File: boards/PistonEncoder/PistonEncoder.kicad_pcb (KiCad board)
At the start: 2 copper layers, 150 x 100 mm, 32 parts, among them J1 ISP, J2 Ext, J3 PWR, J4 LED1, J5 LED2, J6 Pistons1, J7 Pistons2, J8 BoardCon, Q1 BC547, U1 ATmega48-20P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

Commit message: Added bypass caps to power supplies, use cheaper MAX232 IC.
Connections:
- U2 pad 10: /LED_PWR -> unconnected-(U2-COM-Pad10)
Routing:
- net /LED_PWR: track 202.2 -> 195.2 mm
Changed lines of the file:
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@@
 	(net 75 "unconnected-(U5-O6-Pad9)")
 	(net 76 "Net-(Q1-B)")
+	(net 77 "unconnected-(U2-COM-Pad10)")
 	(footprint "Connector_IDC:IDC-Header_2x05_P2.54mm_Vertical"
 		(layer "F.Cu")
@@
 			(layers "*.Cu" "*.Mask")
 			(remove_unused_layers no)
-			(net 22 "/LED_PWR")
+			(net 77 "unconnected-(U2-COM-Pad10)")
 			(pinfunction "COM")
-			(pintype "passive")
+			(pintype "passive+no_connect")
 		)
 		(pad "11" thru_hole oval
@@
 		(tags "TO-92L Inline Wide transistor")
 		(property "Reference" "Q1"
-			(at 2.54 -3.56 270)
+			(at 2.54 -3.56 -90)
 			(layer "F.SilkS")
 			(effects
@@
 		)
 		(property "Value" "BC547"
-			(at 2.54 2.79 270)
+			(at 2.54 2.79 -90)
 			(layer "F.Fab")
 			(effects
@@
 		)
 		(fp_text user "${REFERENCE}"
-			(at 2.54 0 270)
+			(at 2.54 0 -90)
 			(layer "F.Fab")
 			(effects
@@
 	)
 	(segment
-		(start 112.776 59.896)
-		(end 121.158 68.278)
+		(start 115.062 99.187)
+		(end 119.507 99.187)
 		(width 0.6)
 		(layer "B.Cu")
@@
 	)
 	(segment
-		(start 134.62 58.42)
-		(end 133.096 56.896)
-		(width 0.6)
-		(layer "B.Cu")
-		(net 22)
-	)
-	(segment
-		(start 113.538 106.68)
-		(end 113.538 105.41)
+		(start 119.507 99.187)
+		(end 121.158 97.536)
 		(width 0.6)
 		(layer "B.Cu")
@@
 	)
 	(segment
-		(start 109.22 101.092)
-		(end 109.22 99.06)
+		(start 121.158 97.536)
+		(end 121.158 68.278)
 		(width 0.6)
 		(layer "B.Cu")
@@
 	)
 	(segment
-		(start 119.634 99.06)
-		(end 109.22 99.06)
+		(start 113.538 100.711)
+		(end 115.062 99.187)
 		(width 0.6)
 		(layer "B.Cu")
@@
 	)
 	(segment
-		(start 112.776 56.896)
-		(end 112.776 59.896)
+		(start 205.74 130.115919)
+		(end 200.338081 124.714)
 		(width 0.6)
 		(layer "B.Cu")
@@
 	(segment
 		(start 133.096 56.896)
-		(end 112.776 56.896)
+		(end 134.62 58.42)
 		(width 0.6)
 		(layer "B.Cu")
@@
 	)
 	(segment
-		(start 121.158 97.536)
-		(end 119.634 99.06)
+		(start 205.74 131.318)
+		(end 205.74 130.115919)
 		(width 0.6)
 		(layer "B.Cu")
@@
 	)
 	(segment
-		(start 121.158 68.278)
-		(end 121.158 97.536)
+		(start 112.776 59.896)
+		(end 112.776 56.896)
 		(width 0.6)
 		(layer "B.Cu")
@@
 	)
 	(segment
-		(start 205.74 130.115919)
-		(end 200.338081 124.714)
+		(start 121.158 68.278)
+		(end 112.776 59.896)
 		(width 0.6)
 		(layer "B.Cu")
@@
 	)
 	(segment
-		(start 205.74 131.318)
-		(end 205.74 130.115919)
+		(start 112.776 56.896)
+		(end 133.096 56.896)
 		(width 0.6)
 		(layer "B.Cu")
@@
 	)
 	(segment
-		(start 113.538 105.41)
-		(end 109.22 101.092)
+		(start 200.338081 124.714)
+		(end 113.538 124.714)
 		(width 0.6)
 		(layer "B.Cu")
@@
 	)
 	(segment
-		(start 200.338081 124.714)
-		(end 113.538 124.714)
+		(start 113.538 106.68)
+		(end 113.538 100.711)
 		(width 0.6)
 		(layer "B.Cu")

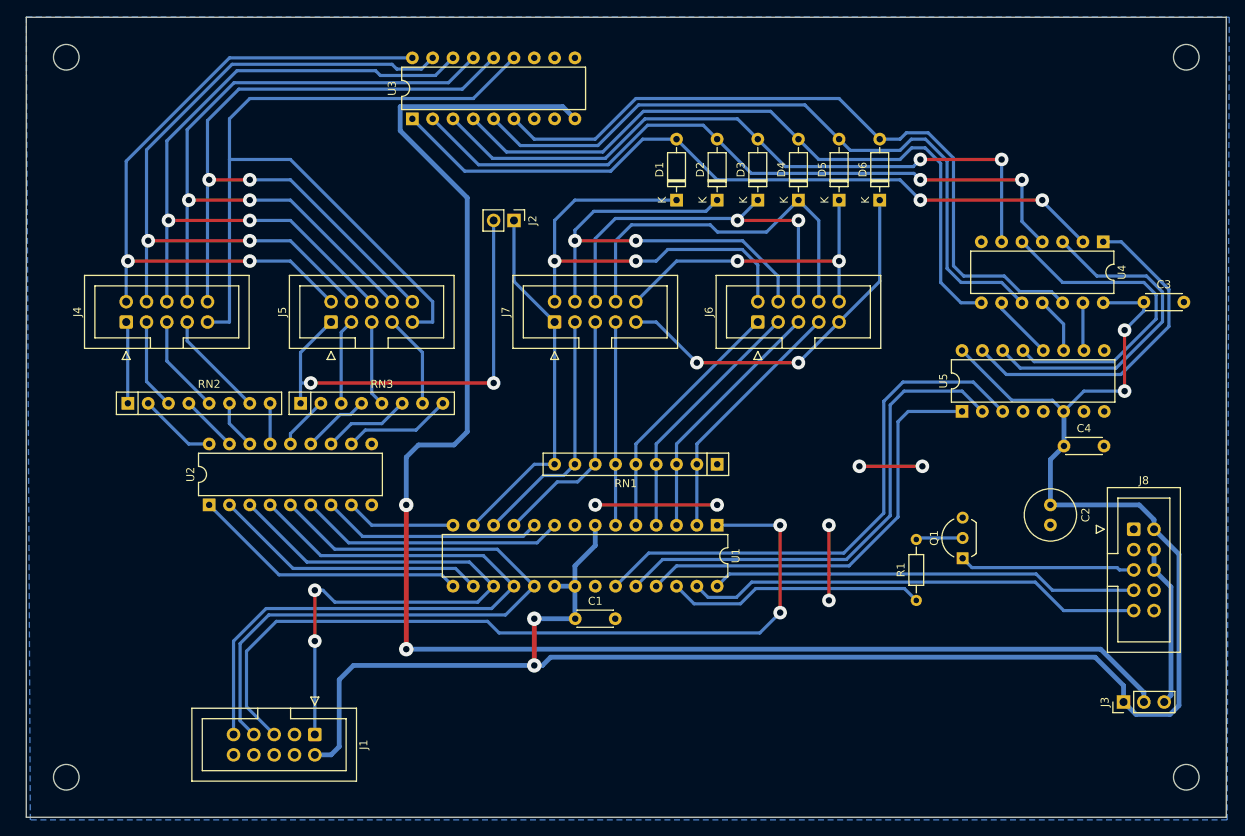
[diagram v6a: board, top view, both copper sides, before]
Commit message: Updated design rules to 0.32mm template and exported Gerber files
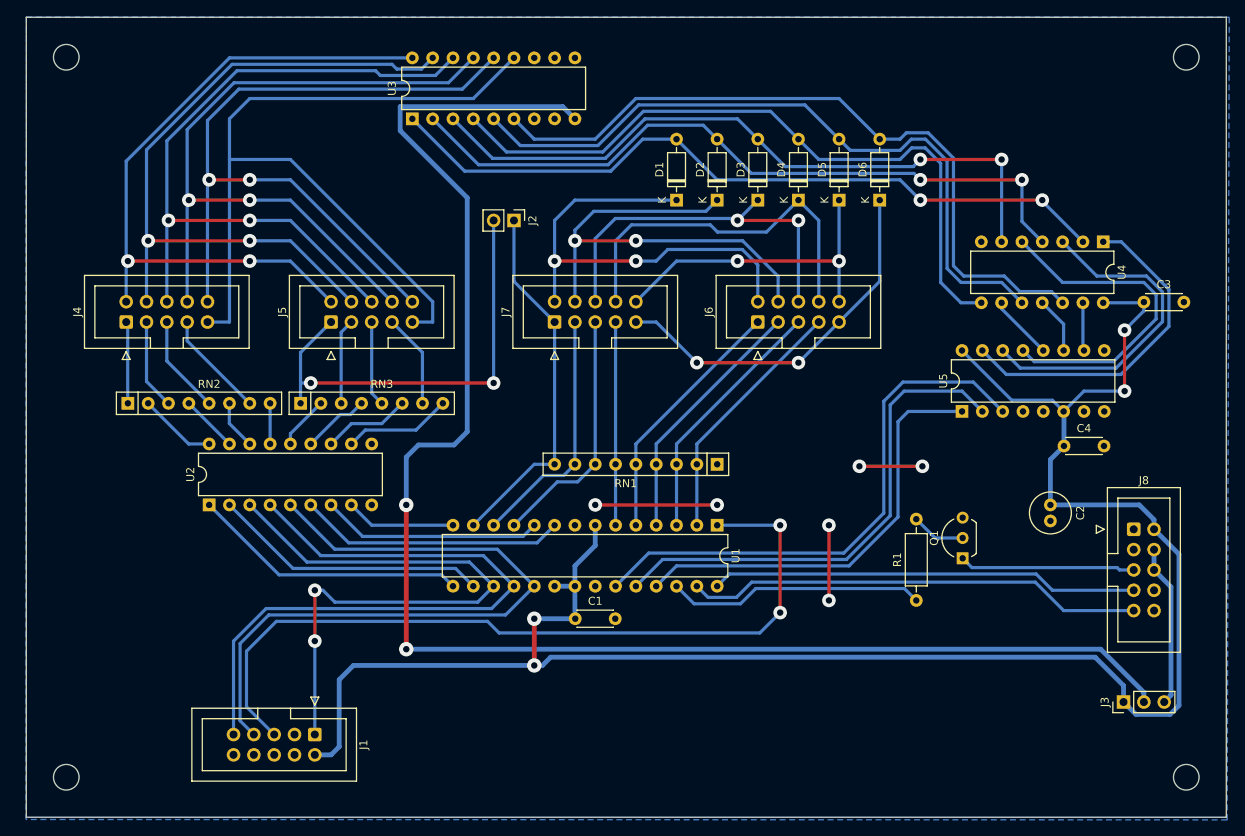
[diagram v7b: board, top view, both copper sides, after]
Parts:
- C2: footprint Capacitor_THT:C_Radial_D6.3mm_H7.0mm_P2.50mm -> Capacitor_THT:C_Radial_D5.0mm_H11.0mm_P2.00mm
- R1: footprint Resistor_THT:R_Axial_DIN0204_L3.6mm_D1.6mm_P7.62mm_Horizontal -> Resistor_THT:R_Axial_DIN0207_L6.3mm_D2.5mm_P10.16mm_Horizontal
- RN1: value R_Network08 -> 10k
- RN2, RN3: value R_Pack04_SIP_Split -> 330
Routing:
- net Net-(Q1-B): track 5.61 -> 6.77 mm
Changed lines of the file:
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@@
 		(pad_to_mask_clearance 0)
 		(allow_soldermask_bridges_in_footprints no)
-		(aux_axis_origin 66.04 45.72)
+		(aux_axis_origin 66.04 145.72)
 		(pcbplotparams
-			(layerselection 0x00010fc_ffffffff)
+			(layerselection 0x0001060_fffffffe)
 			(plot_on_all_layers_selection 0x0000000_00000000)
 			(disableapertmacros no)
@@
 			(viasonmask no)
 			(mode 1)
-			(useauxorigin no)
+			(useauxorigin yes)
 			(hpglpennumber 1)
 			(hpglpenspeed 20)
@@
 			(outputformat 1)
 			(mirror no)
-			(drillshape 1)
+			(drillshape 0)
 			(scaleselection 1)
-			(outputdirectory "")
+			(outputdirectory "gerber/")
 		)
 	)
@@
 			)
 		)
-		(property "Value" "R_Pack04_SIP_Split"
+		(property "Value" "330"
 			(at 10.16 2.4 0)
 			(layer "F.Fab")
@@
 		)
 	)
-	(footprint "Resistor_THT:R_Axial_DIN0204_L3.6mm_D1.6mm_P7.62mm_Horizontal"
+	(footprint "Resistor_THT:R_Axial_DIN0207_L6.3mm_D2.5mm_P10.16mm_Horizontal"
 		(layer "F.Cu")
 		(at 177.292 118.618 90)
-		(descr "Resistor, Axial_DIN0204 series, Axial, Horizontal, pin pitch=7.62mm, 0.167W, length*diameter=3.6*1.6mm^2, http://cdn-reichelt.de/documents/datenblatt/B400/1_4W%23YAG.pdf")
-		(tags "Resistor Axial_DIN0204 series Axial Horizontal pin pitch 7.62mm 0.167W length 3.6mm diameter 1.6mm")
+		(descr "Resistor, Axial_DIN0207 series, Axial, Horizontal, pin pitch=10.16mm, 0.25W = 1/4W, length*diameter=6.3*2.5mm^2, http://cdn-reichelt.de/documents/datenblatt/B400/1_4W%23YAG.pdf")
+		(tags "Resistor Axial_DIN0207 series Axial Horizontal pin pitch 10.16mm 0.25W = 1/4W length 6.3mm diameter 2.5mm")
 		(property "Reference" "R1"
-			(at 3.81 -1.92 -90)
+			(at 5.08 -2.37 90)
 			(layer "F.SilkS")
 			(effects
@@
 		)
 		(property "Value" "4k7"
-			(at 3.81 1.92 -90)
+			(at 5.08 2.37 90)
 			(layer "F.Fab")
 			(effects
@@
 			)
 		)
-		(property "Footprint" "Resistor_THT:R_Axial_DIN0204_L3.6mm_D1.6mm_P7.62mm_Horizontal"
+		(property "Footprint" "Resistor_THT:R_Axial_DIN0207_L6.3mm_D2.5mm_P10.16mm_Horizontal"
 			(at 0 0 90)
 			(unlocked yes)
@@
 		(attr through_hole)
 		(fp_line
-			(start 5.73 -0.92)
-			(end 1.89 -0.92)
+			(start 8.35 -1.37)
+			(end 1.81 -1.37)
 			(stroke
 				(width 0.12)
@@
 		)
 		(fp_line
-			(start 1.89 -0.92)
-			(end 1.89 0.92)
+			(start 1.81 -1.37)
+			(end 1.81 1.37)
 			(stroke
 				(width 0.12)
@@
 		)
 		(fp_line
-			(start 6.68 0)
-			(end 5.73 0)
+			(start 9.12 0)
+			(end 8.35 0)
 			(stroke
 				(width 0.12)
@@
 		)
 		(fp_line
-			(start 0.94 0)
-			(end 1.89 0)
+			(start 1.04 0)
+			(end 1.81 0)
 			(stroke
 				(width 0.12)
@@
 		)
 		(fp_line
-			(start 5.73 0.92)
-			(end 5.73 -0.92)
+			(start 8.35 1.37)
+			(end 8.35 -1.37)
 			(stroke
 				(width 0.12)
@@
 		)
 		(fp_line
-			(start 1.89 0.92)
-			(end 5.73 0.92)
+			(start 1.81 1.37)
+			(end 8.35 1.37)
 			(stroke
 				(width 0.12)
@@
 		)
 		(fp_line
-			(start 8.57 -1.05)
-			(end -0.95 -1.05)
+			(start 11.21 -1.5)
+			(end -1.05 -1.5)
 			(stroke
 				(width 0.05)
@@
 		)
 		(fp_line
-			(start -0.95 -1.05)
-			(end -0.95 1.05)
+			(start -1.05 -1.5)
+			(end -1.05 1.5)
 			(stroke
 				(width 0.05)
@@
 		)
 		(fp_line
-			(start 8.57 1.05)
-			(end 8.57 -1.05)
+			(start 11.21 1.5)
+			(end 11.21 -1.5)
 			(stroke
 				(width 0.05)
@@
 		)
 		(fp_line
-			(start -0.95 1.05)
-			(end 8.57 1.05)
+			(start -1.05 1.5)
+			(end 11.21 1.5)
 			(stroke
 				(width 0.05)
@@
 		)
 		(fp_line
-			(start 5.61 -0.8)
-			(end 2.01 -0.8)
+			(start 8.23 -1.25)
+			(end 1.93 -1.25)
 			(stroke
 				(width 0.1)
@@
 		)
 		(fp_line
-			(start 2.01 -0.8)
-			(end 2.01 0.8)
+			(start 1.93 -1.25)
+			(end 1.93 1.25)
 			(stroke
 				(width 0.1)
@@
 		)
 		(fp_line
-			(start 7.62 0)
-			(end 5.61 0)
+			(start 10.16 0)
+			(end 8.23 0)
 			(stroke
 				(width 0.1)
@@
 		(fp_line
 			(start 0 0)
-			(end 2.01 0)
+			(end 1.93 0)
 			(stroke
 				(width 0.1)
@@
 		)
 		(fp_line
-			(start 5.61 0.8)
-			(end 5.61 -0.8)
+			(start 8.23 1.25)
+			(end 8.23 -1.25)
 			(stroke
 				(width 0.1)
@@
 		)
 		(fp_line
-			(start 2.01 0.8)
-			(end 5.61 0.8)
+			(start 1.93 1.25)
+			(end 8.23 1.25)
 			(stroke
 				(width 0.1)
@@
 		)
 		(fp_text user "${REFERENCE}"
-			(at 3.81 0 -90)
+			(at 5.08 0 90)
 			(layer "F.Fab")
 			(effects
 				(font
-					(size 0.72 0.72)
-					(thickness 0.108)
+					(size 1 1)
+					(thickness 0.15)
 				)
 			)
@@
 		(pad "1" thru_hole circle
 			(at 0 0 90)
-			(size 1.4 1.4)
-			(drill 0.7)
+			(size 1.6 1.6)
+			(drill 0.8)
 			(layers "*.Cu" "*.Mask")
 			(remove_unused_layers no)
@@
 		)
 		(pad "2" thru_hole oval
-			(at 7.62 0 90)
-			(size 1.4 1.4)
-			(drill 0.7)
+			(at 10.16 0 90)
+			(size 1.6 1.6)
+			(drill 0.8)
 			(layers "*.Cu" "*.Mask")
 			(remove_unused_layers no)
@@
 			(pintype "passive")
 		)
-		(model "${KICAD6_3DMODEL_DIR}/Resistor_THT.3dshapes/R_Axial_DIN0204_L3.6mm_D1.6mm_P7.62mm_Horizontal.wrl"
+		(model "${KICAD8_3DMODEL_DIR}/Resistor_THT.3dshapes/R_Axial_DIN0207_L6.3mm_D2.5mm_P10.16mm_Horizontal.wrl"
 			(offset
 				(xyz 0 0 0)
@@
 			)
 		)
-		(property "Value" "R_Network08"
+		(property "Value" "10k"
 			(at 11.43 2.4 0)
 			(layer "F.Fab")
@@
 		)
 	)
-	(footprint "Capacitor_THT:C_Radial_D6.3mm_H7.0mm_P2.50mm"
+	(footprint "Capacitor_THT:C_Radial_D5.0mm_H11.0mm_P2.00mm"
 		(layer "F.Cu")
 		(at 194.056 106.68 -90)
-		(descr "C, Radial series, Radial, pin pitch=2.50mm, diameter=6.3mm, height=7mm, Non-Polar Electrolytic Capacitor")
-		(tags "C Radial series Radial pin pitch 2.50mm diameter 6.3mm height 7mm Non-Polar Electrolytic Capacitor")
+		(descr "C, Radial series, Radial, pin pitch=2.00mm, diameter=5mm, height=11mm, Non-Polar Electrolytic Capacitor")
+		(tags "C Radial series Radial pin pitch 2.00mm diameter 5mm height 11mm Non-Polar Electrolytic Capacitor")
 		(property "Reference" "C2"
-			(at 1.25 -4.4 90)
+			(at 1 -3.75 -90)
 			(layer "F.SilkS")
 			(effects
@@
 		)
 		(property "Value" "10uF"
-			(at 1.25 4.4 90)
+			(at 1 3.75 -90)
 			(layer "F.Fab")
 			(effects
@@
 			)
 		)
-		(property "Footprint" "Capacitor_THT:C_Radial_D6.3mm_H7.0mm_P2.50mm"
+		(property "Footprint" "Capacitor_THT:C_Radial_D5.0mm_H11.0mm_P2.00mm"
 			(at 0 0 -90)
 			(unlocked yes)
@@
 		(attr through_hole)
 		(fp_circle
-			(center 1.25 0)
-			(end 4.52 0)
+			(center 1 0)
+			(end 3.62 0)
 			(stroke
 				(width 0.12)
@@
 		)
 		(fp_circle
-			(center 1.25 0)
-			(end 4.65 0)
+			(center 1 0)
+			(end 3.75 0)
 			(stroke
 				(width 0.05)
@@
 		)
 		(fp_circle
-			(center 1.25 0)
-			(end 4.4 0)
+			(center 1 0)
+			(end 3.5 0)
 			(stroke
 				(width 0.1)
@@
 		)
 		(fp_text user "${REFERENCE}"
-			(at 1.25 0 90)
+			(at 1 0 -90)
 			(layer "F.Fab")
 			(effects
@@
 		)
 		(pad "2" thru_hole circle
-			(at 2.5 0 270)
+			(at 2 0 270)
 			(size 1.6 1.6)
 			(drill 0.8)
@@
 			(pintype "passive")
 		)
-		(model "${KICAD6_3DMODEL_DIR}/Capacitor_THT.3dshapes/C_Radial_D6.3mm_H7.0mm_P2.50mm.wrl"
+		(model "${KICAD8_3DMODEL_DIR}/Capacitor_THT.3dshapes/C_Radial_D5.0mm_H11.0mm_P2.00mm.wrl"
 			(offset
 				(xyz 0 0 0)
@@
 			)
 		)
-		(property "Value" "R_Pack04_SIP_Split"
+		(property "Value" "330"
 			(at 10.16 2.4 0)
 			(layer "F.Fab")
@@
 	(segment
 		(start 183.086 110.812)
-		(end 177.478 110.812)
+		(end 179.646 110.812)
+		(width 0.4)
+		(layer "B.Cu")
+		(net 76)
+	)
+	(segment
+		(start 179.646 110.812)
+		(end 177.292 108.458)
 		(width 0.4)
 		(layer "B.Cu")
@@
 		(polygon
 			(pts
-				(xy 66.04 45.72) (xy 216.408 45.72) (xy 216.154 146.05) (xy 66.548 146.05)
+				(xy 66.04 45.72) (xy 216.408 45.72) (xy 216.154 146.05) (xy 66 146)
 			)
 		)
